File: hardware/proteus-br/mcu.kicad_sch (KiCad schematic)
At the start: 40 parts, among them J1 Micro_SD_Card, J1501 USB_B, J1502 Conn_02x05_Odd_Even, SW1501 SW_Push, SW1502 SW_Push, U1501 STM32F427ZGT6, U1502 USBLC6-2SC6, U8 REF3333, Y1501 8MHz

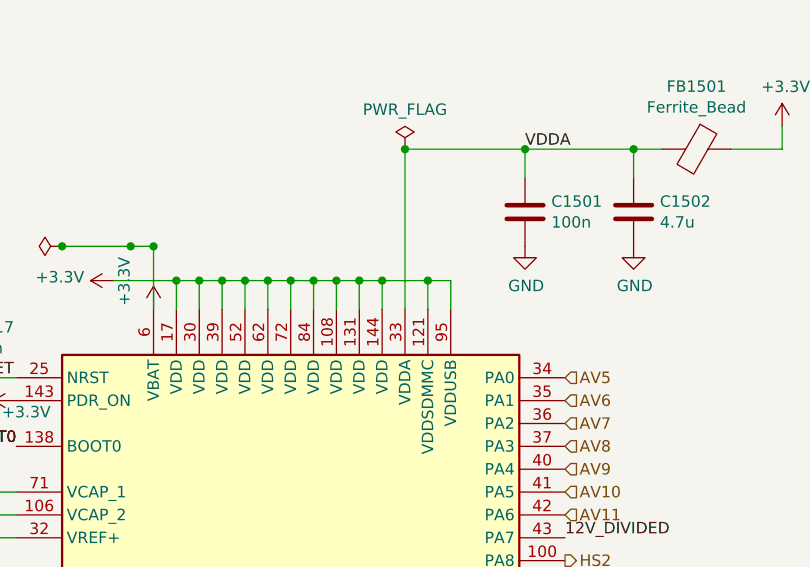
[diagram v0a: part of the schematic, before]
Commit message: proteus-br: title blocks v1 + PWR_FLAG no VDDA (mcu/psu/lowside atualizados)
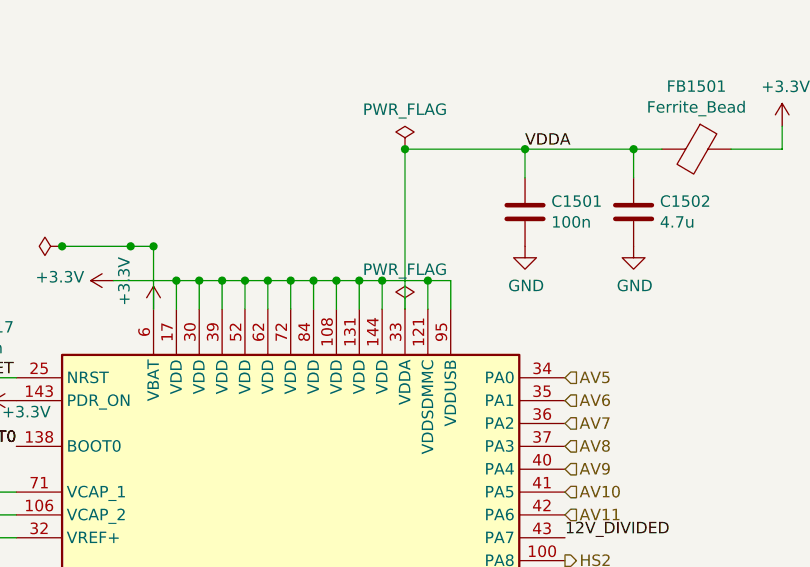
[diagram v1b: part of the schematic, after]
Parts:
- C1521, C1522: footprint Capacitor_SMD:C_0402_1005Metric -> Capacitor_SMD:C_0603_1608Metric
- D1501: LCSC C85364 -> C13612; MFN (none) -> Semtech; MPN (none) -> SRV05-4.TCT
- D1506: LCSC C72043 -> C72038; MFN (none) -> Hubei KENTO; MPN (none) -> KT-0603R-O
- R1501, R1502, R1504, R1511, R1513: footprint Resistor_SMD:R_0402_1005Metric -> Resistor_SMD:R_0603_1608Metric
- U1501: MFN (none) -> STMicroelectronics; MPN (none) -> STM32F427ZGT6
- U1502: MFN (none) -> STMicroelectronics; MPN (none) -> USBLC6-2SC6
- U8: MFN (none) -> Texas Instruments; MPN (none) -> REF3333AIDBZR
- Y1501: MFN (none) -> Yangxing Tech; MPN (none) -> X50328MSB2GI
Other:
- company: rusEFI -> baseado em rusEFI Proteus v0.7
- title: rusEfi Proteus -> Proteus-BR — mcu
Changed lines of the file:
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@@
   (paper "A3")
   (title_block
-    (title "rusEfi Proteus")
-    (date "2022-04-09")
-    (rev "v0.7")
-    (company "rusEFI")
+    (title "Proteus-BR — mcu")
+    (date "2026-06-11")
+    (rev "v1")
+    (company "baseado em rusEFI Proteus v0.7")
     (comment 1 "github.com/mck1117/proteus")
     (comment 2 "rusefi.com/s/proteus")
@@
     (property "PN" "STM32F767ZIT6" (at 134.62 159.385 0) (effects (font (size 1.27 1.27)) hide))
     (property "LCSC" "C117816" (at 134.62 159.385 0) (effects (font (size 1.27 1.27)) hide))
+    (property "MFN" "STMicroelectronics" (at 134.62 163.83 0) (effects (font (size 1.27 1.27)) hide))
+    (property "MPN" "STM32F427ZGT6" (at 134.62 163.83 0) (effects (font (size 1.27 1.27)) hide))
     (pin "1")
     (pin "10")
@@
     (property "Reference" "R1502" (at 81.915 70.3072 90) (effects (font (size 1.27 1.27))))
     (property "Value" "10k" (at 81.915 72.6186 90) (effects (font (size 1.27 1.27))))
-    (property "Footprint" "Resistor_SMD:R_0402_1005Metric"
+    (property "Footprint" "Resistor_SMD:R_0603_1608Metric"
       (at 81.915 73.787 90)
       (effects (font (size 1.27 1.27)) hide)
@@
     (property "Reference" "C1521" (at 75.565 106.045 90) (effects (font (size 1.27 1.27))))
     (property "Value" "33p" (at 75.565 111.125 90) (effects (font (size 1.27 1.27))))
-    (property "Footprint" "Capacitor_SMD:C_0402_1005Metric"
+    (property "Footprint" "Capacitor_SMD:C_0603_1608Metric"
       (at 75.565 108.585 0)
       (effects (font (size 1.27 1.27)) hide)
@@
     (property "Reference" "C1522" (at 75.565 113.665 90) (effects (font (size 1.27 1.27))))
     (property "Value" "33p" (at 75.565 118.745 90) (effects (font (size 1.27 1.27))))
-    (property "Footprint" "Capacitor_SMD:C_0402_1005Metric"
+    (property "Footprint" "Capacitor_SMD:C_0603_1608Metric"
       (at 75.565 116.205 0)
       (effects (font (size 1.27 1.27)) hide)
@@
     )
     (property "Value" "100k" (at 305.943 95.123 0) (effects (font (size 1.27 1.27)) (justify left)))
-    (property "Footprint" "Resistor_SMD:R_0402_1005Metric"
+    (property "Footprint" "Resistor_SMD:R_0603_1608Metric"
       (at 302.387 93.98 90)
       (effects (font (size 1.27 1.27)) hide)
@@
     )
     (property "Value" "10k" (at 298.958 45.593 0) (effects (font (size 1.27 1.27)) (justify left)))
-    (property "Footprint" "Resistor_SMD:R_0402_1005Metric"
+    (property "Footprint" "Resistor_SMD:R_0603_1608Metric"
       (at 295.402 44.45 90)
       (effects (font (size 1.27 1.27)) hide)
@@
     )
     (property "Datasheet" "~" (at 211.455 203.2 0) (effects (font (size 1.27 1.27)) hide))
-    (property "LCSC" "C72043" (at 211.455 203.2 0) (effects (font (size 1.27 1.27)) hide))
+    (property "LCSC" "C72038" (at 211.455 203.2 0) (effects (font (size 1.27 1.27)) hide))
     (property "LCSC_ext" "0" (at 211.455 203.2 0) (effects (font (size 1.27 1.27)) hide))
+    (property "MFN" "Hubei KENTO" (at 211.455 198.755 0) (effects (font (size 1.27 1.27)) hide))
+    (property "MPN" "KT-0603R-O" (at 211.455 198.755 0) (effects (font (size 1.27 1.27)) hide))
     (pin "1")
     (pin "2")
@@
     (property "Reference" "R1511" (at 219.075 197.9422 90) (effects (font (size 1.27 1.27))))
     (property "Value" "1k" (at 219.075 200.2536 90) (effects (font (size 1.27 1.27))))
-    (property "Footprint" "Resistor_SMD:R_0402_1005Metric"
+    (property "Footprint" "Resistor_SMD:R_0603_1608Metric"
       (at 219.075 201.422 90)
       (effects (font (size 1.27 1.27)) hide)
@@
     (property "Reference" "R1513" (at 199.39 154.94 90) (effects (font (size 1.27 1.27))))
     (property "Value" "10k" (at 201.295 154.94 90) (effects (font (size 1.27 1.27))))
-    (property "Footprint" "Resistor_SMD:R_0402_1005Metric"
+    (property "Footprint" "Resistor_SMD:R_0603_1608Metric"
       (at 201.295 154.94 0)
       (effects (font (size 1.27 1.27)) hide)
@@
     (property "LCSC" "C115962" (at 90.805 112.395 0) (effects (font (size 1.27 1.27)) hide))
     (property "LCSC_ext" "0" (at 90.805 112.395 0) (effects (font (size 1.27 1.27)) hide))
+    (property "MFN" "Yangxing Tech" (at 94.1324 111.2266 0) (effects (font (size 1.27 1.27)) hide))
+    (property "MPN" "X50328MSB2GI" (at 94.1324 111.2266 0) (effects (font (size 1.27 1.27)) hide))
     (pin "1")
     (pin "2")
@@
       (effects (font (size 1.27 1.27)) hide)
     )
-    (property "LCSC" "C85364" (at 349.25 41.91 0) (effects (font (size 1.27 1.27)) hide))
+    (property "LCSC" "C13612" (at 349.25 41.91 0) (effects (font (size 1.27 1.27)) hide))
     (property "LCSC_ext" "0" (at 349.25 41.91 0) (effects (font (size 1.27 1.27)) hide))
+    (property "MFN" "Semtech" (at 343.535 29.845 0) (effects (font (size 1.27 1.27)) hide))
+    (property "MPN" "SRV05-4.TCT" (at 343.535 29.845 0) (effects (font (size 1.27 1.27)) hide))
     (pin "1")
     (pin "2")
@@
     (property "LCSC_ext" "1" (at 40.64 100.33 0) (effects (font (size 1.27 1.27)) hide))
     (property "PN" "REF3033" (at 40.64 100.33 0) (effects (font (size 1.27 1.27)) hide))
+    (property "MFN" "Texas Instruments" (at 34.8234 99.1616 0) (effects (font (size 1.27 1.27)) hide))
+    (property "MPN" "REF3333AIDBZR" (at 34.8234 99.1616 0) (effects (font (size 1.27 1.27)) hide))
     (pin "1")
     (pin "2")
@@
     (property "LCSC_ext" "1" (at 281.94 111.125 0) (effects (font (size 1.27 1.27)) hide))
     (property "possible_not_ext" "1" (at 281.94 111.125 0) (effects (font (size 1.27 1.27)) hide))
+    (property "MFN" "STMicroelectronics" (at 285.75 101.6 0) (effects (font (size 1.27 1.27)) hide))
+    (property "MPN" "USBLC6-2SC6" (at 285.75 101.6 0) (effects (font (size 1.27 1.27)) hide))
     (pin "1")
     (pin "2")
@@
     (effects (font (size 1.27 1.27)) (justify left bottom))
   )
+  (symbol
+    (lib_id "power:PWR_FLAG")
+    (at 147.32 67.945 0)
+    (unit 1)
+    (in_bom yes)
+    (on_board yes)
+    (dnp no)
+    (property "Reference" "#PWR09001" (at 147.32 66.04 0) (effects (font (size 1.27 1.27)) hide))
+    (property "Value" "PWR_FLAG" (at 147.32 63.551 0) (effects (font (size 1.27 1.27))))
+    (property "Footprint" "" (at 147.32 67.945 0) (effects (font (size 1.27 1.27)) hide))
+    (property "Datasheet" "~" (at 147.32 67.945 0) (effects (font (size 1.27 1.27)) hide))
+    (pin "1")
+    (instances
+      (project "proteus-br"
+        (path "/da96cc1d-20c0-47ba-9881-2a73783a20fb/00000000-0000-0000-0000-00005d99e6ee"
+          (reference "#PWR09001")
+          (unit 1)
+        )
+      )
+    )
+  )
 )
